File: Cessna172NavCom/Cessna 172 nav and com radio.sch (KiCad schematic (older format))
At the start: 33 parts, among them J2 USB_B_Micro, J8 Conn_02x20_Odd_Even, SW1 SW_Push, SW2 SW_Push, SW3 SW_Push, SW4 SW_Push, SW5 SW_Push, SW6 SW_Push

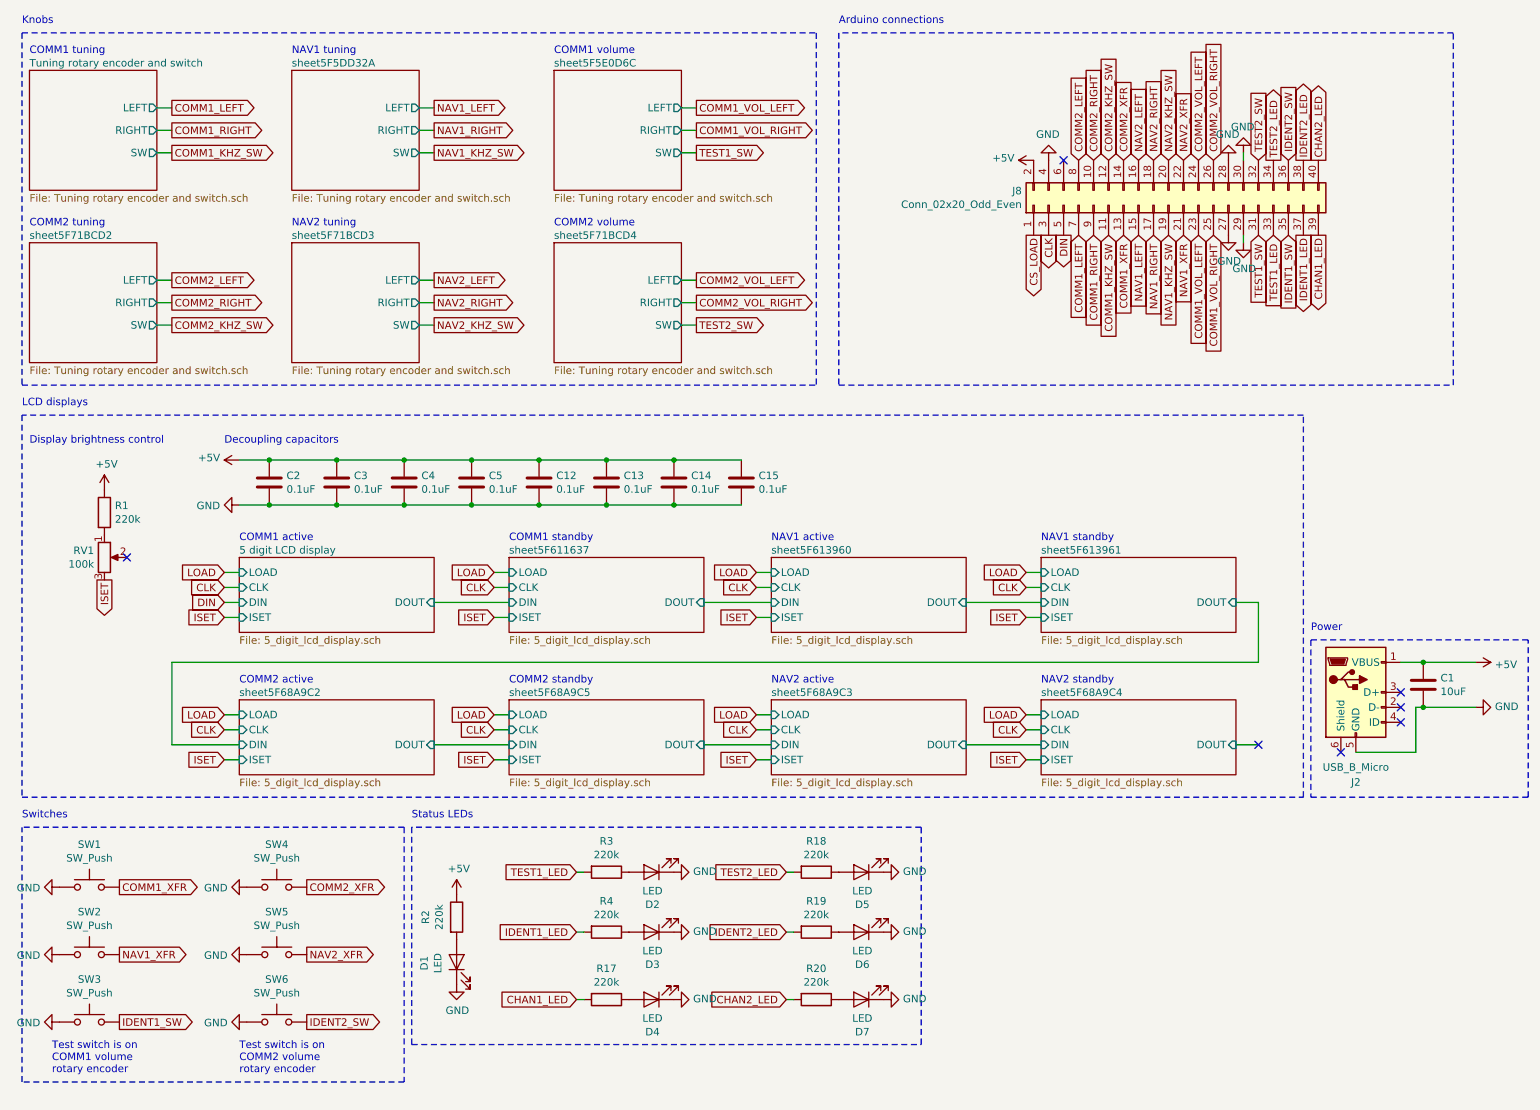
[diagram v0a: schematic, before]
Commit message: Remove unnecessary items, rename some of the nets
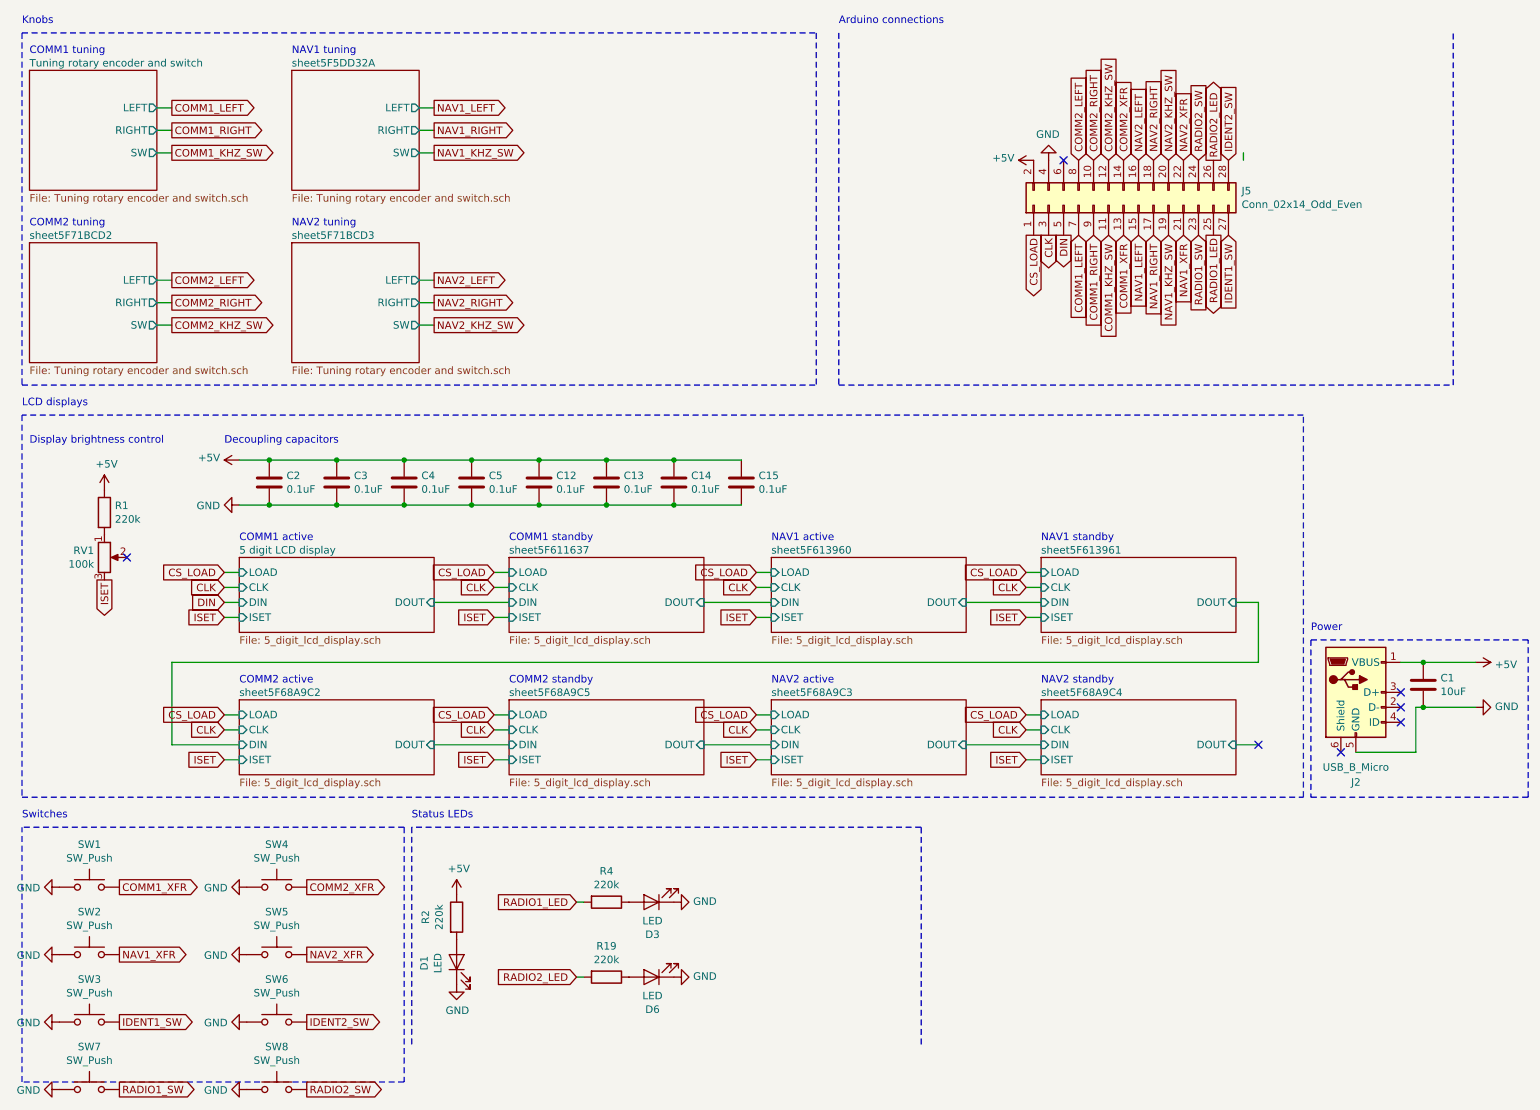
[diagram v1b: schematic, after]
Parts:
- removed D2, D4, D5, D7: LED, LED_THT:LED_D5.0mm, symbol Device:LED
- removed J8: Conn_02x20_Odd_Even, SamacSys_Parts:SAMTEC-TST-120-01-X-D, symbol Connector_Generic:Conn_02x20_Odd_Even
- removed R17, R18, R20, R3: 220k, Resistor_SMD:R_0805_2012Metric_Pad1.15x1.40mm_HandSolder, symbol Device:R
- added J5: Conn_02x14_Odd_Even, Connector_PinHeader_2.54mm:PinHeader_2x14_P2.54mm_Vertical, symbol Connector_Generic:Conn_02x14_Odd_Even
- added SW7, SW8: SW_Push, Button_Switch_THT:SW_PUSH_6mm_H8mm, symbol Switch:SW_Push
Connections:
- net +5V: now also J5.2 (Pin_2)
- net CLK: now also J5.3 (Pin_3)
- net COMM1_KHZ_SW: now also J5.11 (Pin_11)
- net COMM1_LEFT: now also J5.7 (Pin_7)
- net COMM1_RIGHT: now also J5.9 (Pin_9)
- net COMM1_XFR: now also J5.13 (Pin_13)
- net COMM2_KHZ_SW: now also J5.12 (Pin_12)
- net COMM2_LEFT: now also J5.8 (Pin_8)
- net COMM2_RIGHT: now also J5.10 (Pin_10)
- net COMM2_XFR: now also J5.14 (Pin_14)
- net CS_LOAD: now also J5.1 (Pin_1)
- net DIN: now also J5.5 (Pin_5)
- net GND: now also J5.4 (Pin_4), SW7.1, SW8.1
- net IDENT1_SW: now also J5.27 (Pin_27)
- net IDENT2_SW: now also J5.28 (Pin_28)
- net NAV1_KHZ_SW: now also J5.19 (Pin_19)
- net NAV1_LEFT: now also J5.15 (Pin_15)
- net NAV1_RIGHT: now also J5.17 (Pin_17)
- net NAV1_XFR: now also J5.21 (Pin_21)
- net NAV2_KHZ_SW: now also J5.20 (Pin_20)
- net NAV2_LEFT: now also J5.16 (Pin_16)
- net NAV2_RIGHT: now also J5.18 (Pin_18)
- net NAV2_XFR: now also J5.22 (Pin_22)
- net IDENT1_LED renamed RADIO1_LED
- net RADIO1_LED: now also J5.25 (Pin_25)
- net IDENT2_LED renamed RADIO2_LED
- net RADIO2_LED: now also J5.26 (Pin_26)
- new net RADIO1_SW: J5.23 (Pin_23), SW7.2
- new net RADIO2_SW: J5.24 (Pin_24), SW8.2
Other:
- note removed: "COMM1 volume"
- note removed: "COMM2 volume"
- note removed: "Test switch is on\nCOMM1 volume\nrotary encoder"
- note removed: "Test switch is on\nCOMM2 volume\nrotary encoder"
- moved on the sheet: D3, D6, R19, R4

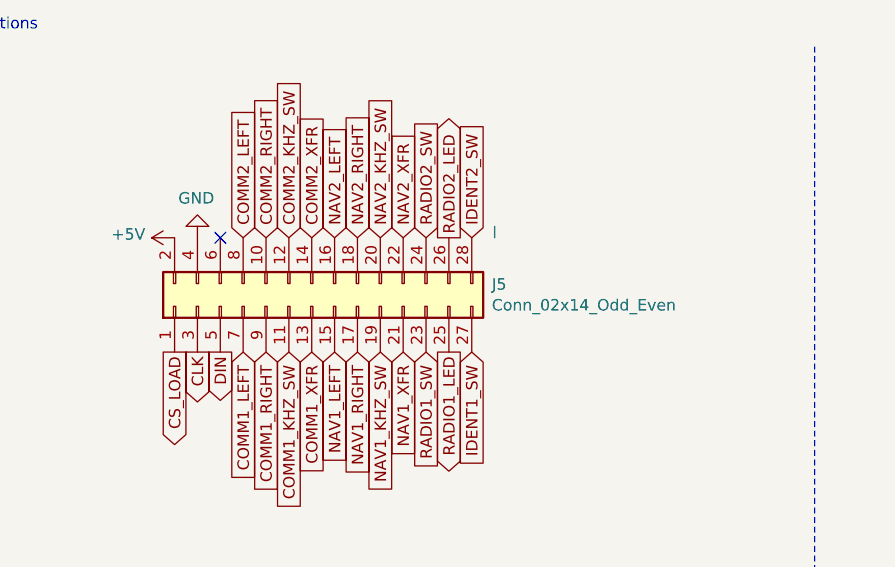
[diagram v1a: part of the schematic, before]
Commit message: Switch to 30 pin connector for availability reasons
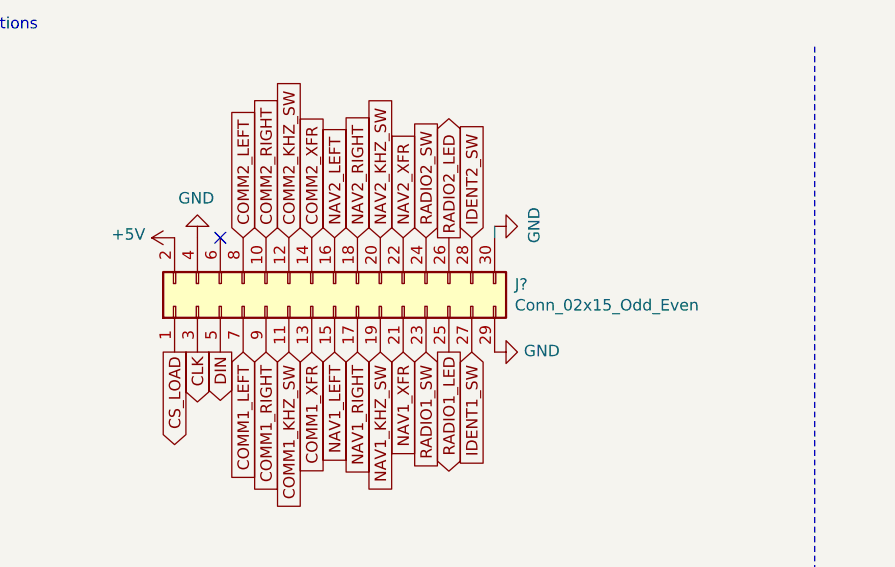
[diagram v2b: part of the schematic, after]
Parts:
- removed J5: Conn_02x14_Odd_Even, Connector_PinHeader_2.54mm:PinHeader_2x14_P2.54mm_Vertical, symbol Connector_Generic:Conn_02x14_Odd_Even
- added J?: Conn_02x15_Odd_Even, symbol Connector_Generic:Conn_02x15_Odd_Even
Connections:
- net +5V: now also J?.2 (Pin_2)
- net CLK: now also J?.3 (Pin_3)
- net COMM1_KHZ_SW: now also J?.11 (Pin_11)
- net COMM1_LEFT: now also J?.7 (Pin_7)
- net COMM1_RIGHT: now also J?.9 (Pin_9)
- net COMM1_XFR: now also J?.13 (Pin_13)
- net COMM2_KHZ_SW: now also J?.12 (Pin_12)
- net COMM2_LEFT: now also J?.8 (Pin_8)
- net COMM2_RIGHT: now also J?.10 (Pin_10)
- net COMM2_XFR: now also J?.14 (Pin_14)
- net CS_LOAD: now also J?.1 (Pin_1)
- net DIN: now also J?.5 (Pin_5)
- net GND: now also J?.29 (Pin_29), J?.30 (Pin_30), J?.4 (Pin_4)
- net IDENT1_SW: now also J?.27 (Pin_27)
- net IDENT2_SW: now also J?.28 (Pin_28)
- net NAV1_KHZ_SW: now also J?.19 (Pin_19)
- net NAV1_LEFT: now also J?.15 (Pin_15)
- net NAV1_RIGHT: now also J?.17 (Pin_17)
- net NAV1_XFR: now also J?.21 (Pin_21)
- net NAV2_KHZ_SW: now also J?.20 (Pin_20)
- net NAV2_LEFT: now also J?.16 (Pin_16)
- net NAV2_RIGHT: now also J?.18 (Pin_18)
- net NAV2_XFR: now also J?.22 (Pin_22)
- net RADIO1_LED: now also J?.25 (Pin_25)
- net RADIO1_SW: now also J?.23 (Pin_23)
- net RADIO2_LED: now also J?.26 (Pin_26)
- net RADIO2_SW: now also J?.24 (Pin_24)
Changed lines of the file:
@@
 $EndComp
 $Comp
-L Connector_Generic:Conn_02x14_Odd_Even J5
-U 1 1 5F6E8F05
-P 7950 1800
-F 0 "J5" V 8046 1012 50  0000 R CNN
-F 1 "Conn_02x14_Odd_Even" V 7955 1012 50  0000 R CNN
-F 2 "Connector_PinHeader_2.54mm:PinHeader_2x14_P2.54mm_Vertical" H 7950 1800 50  0001 C CNN
-F 3 "~" H 7950 1800 50  0001 C CNN
-	1    7950 1800
+L Connector_Generic:Conn_02x15_Odd_Even J?
+U 1 1 5F701A0C
+P 8050 1800
+F 0 "J?" V 8146 1012 50  0000 R CNN
+F 1 "Conn_02x15_Odd_Even" V 8055 1012 50  0000 R CNN
+F 2 "" H 8050 1800 50  0001 C CNN
+F 3 "~" H 8050 1800 50  0001 C CNN
+	1    8050 1800
 	0    -1   -1   0
 $EndComp
+$Comp
+L power:GND #PWR?
+U 1 1 5F705AED
+P 8750 2000
+F 0 "#PWR?" H 8750 1750 50  0001 C CNN
+F 1 "GND" V 8755 1872 50  0000 R CNN
+F 2 "" H 8750 2000 50  0001 C CNN
+F 3 "" H 8750 2000 50  0001 C CNN
+	1    8750 2000
+	0    -1   -1   0
+$EndComp
+$Comp
+L power:GND #PWR?
+U 1 1 5F705602
+P 8750 1450
+F 0 "#PWR?" H 8750 1200 50  0001 C CNN
+F 1 "GND" H 8755 1277 50  0000 C CNN
+F 2 "" H 8750 1450 50  0001 C CNN
+F 3 "" H 8750 1450 50  0001 C CNN
+	1    8750 1450
+	0    -1   -1   0
+$EndComp
